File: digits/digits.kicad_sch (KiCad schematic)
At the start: 265 parts, among them J1 SOLDER, J2 EDGE_CONNECT, Q1 BSS84, Q10 BSS84, Q11 BSS84, Q12 BSS84, Q13 BSS84, Q14 BSS84, Q2 BSS84, Q3 BSS84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

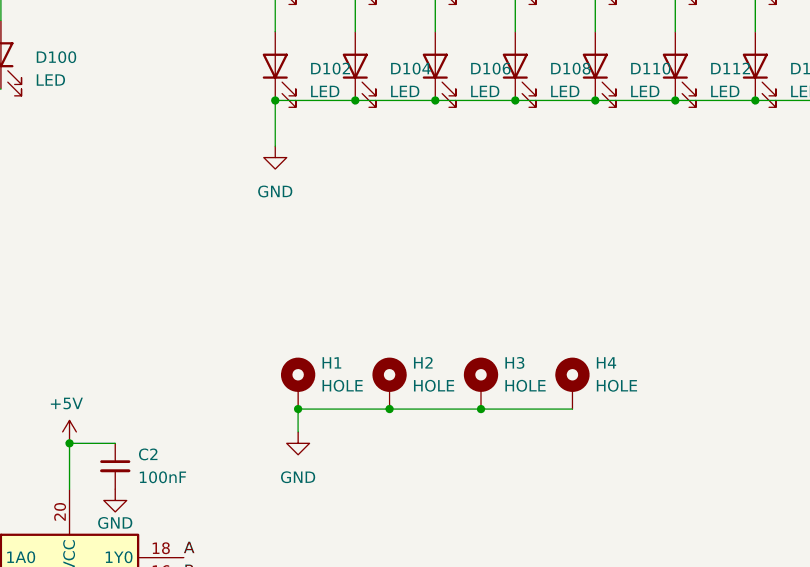
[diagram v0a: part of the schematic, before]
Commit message: Added fiducials, fixed typo on the connector, added the correct origin, added a version number
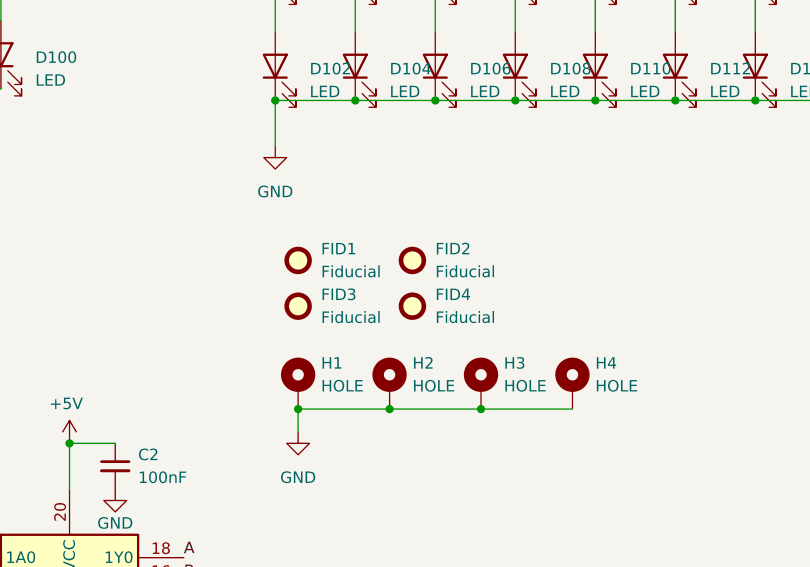
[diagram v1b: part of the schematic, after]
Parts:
- added FID1, FID2, FID3, FID4: Fiducial, Fiducial:Fiducial_1mm_Mask3mm, symbol Mechanical:Fiducial

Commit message: didn't even need that part
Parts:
- removed C2: 100nF, Capacitor_SMD:C_0603_1608Metric, symbol Device:C_Small
- removed U2: 74AHC244, Package_SO:TSSOP-20_4.4x5mm_P0.5mm, symbol 74xx:74AHC244
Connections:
- net A: now also U1.15 (QA)
- net B: now also U1.1 (QB)
- net C: now also U1.2 (QC)
- net D: now also U1.3 (QD)
- net E: now also U1.4 (QE)
- net F: now also U1.5 (QF)
- net G: now also U1.6 (QG)
- net at U1.7 (QH): now also R99.2
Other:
- moved on the sheet: R99
